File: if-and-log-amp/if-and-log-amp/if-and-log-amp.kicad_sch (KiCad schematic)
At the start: 84 parts, among them J301 Coax, J302 SMA Panel Mount, J303 SMA Panel Mount, J304 SMA Panel Mount, J305 Conn_01x03, J306 Conn_01x02, J307 Conn_Coaxial, Q301 2N3904, T301 FT37-43 8:2 t, U301 AD603AQ, U302 L78L05_TO92, U303 LM317L_TO92, U304 ${SIM.PARAMS}, U305 CA3140

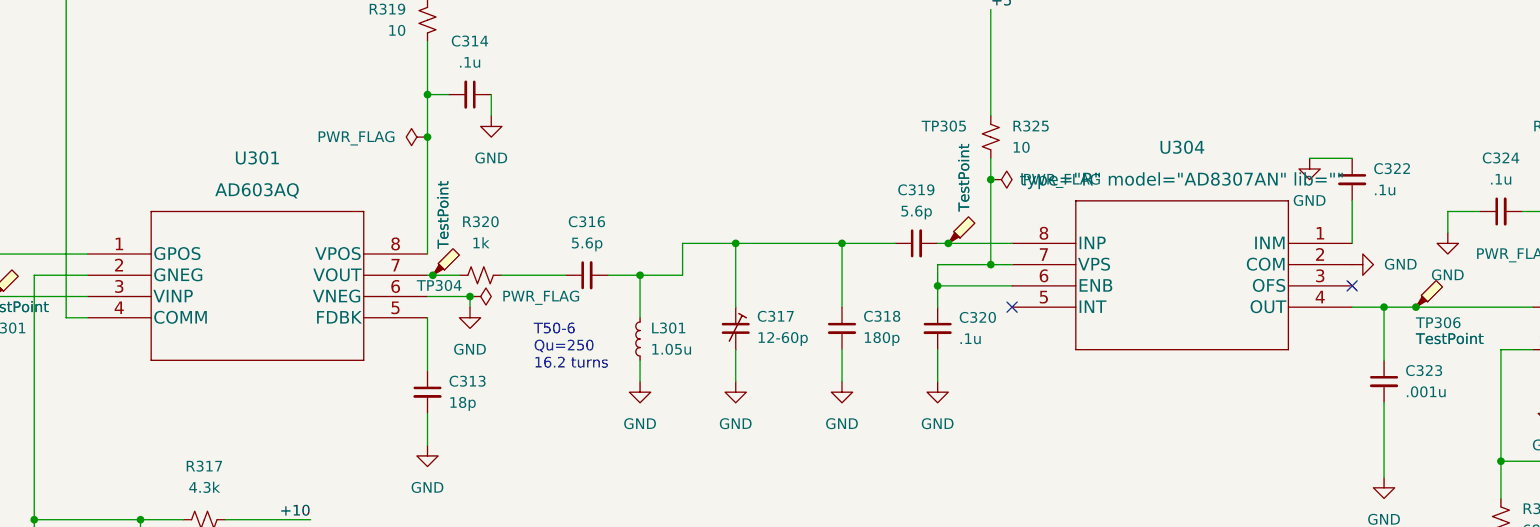
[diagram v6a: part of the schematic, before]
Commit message: Update to timebase and 2lo gerbers
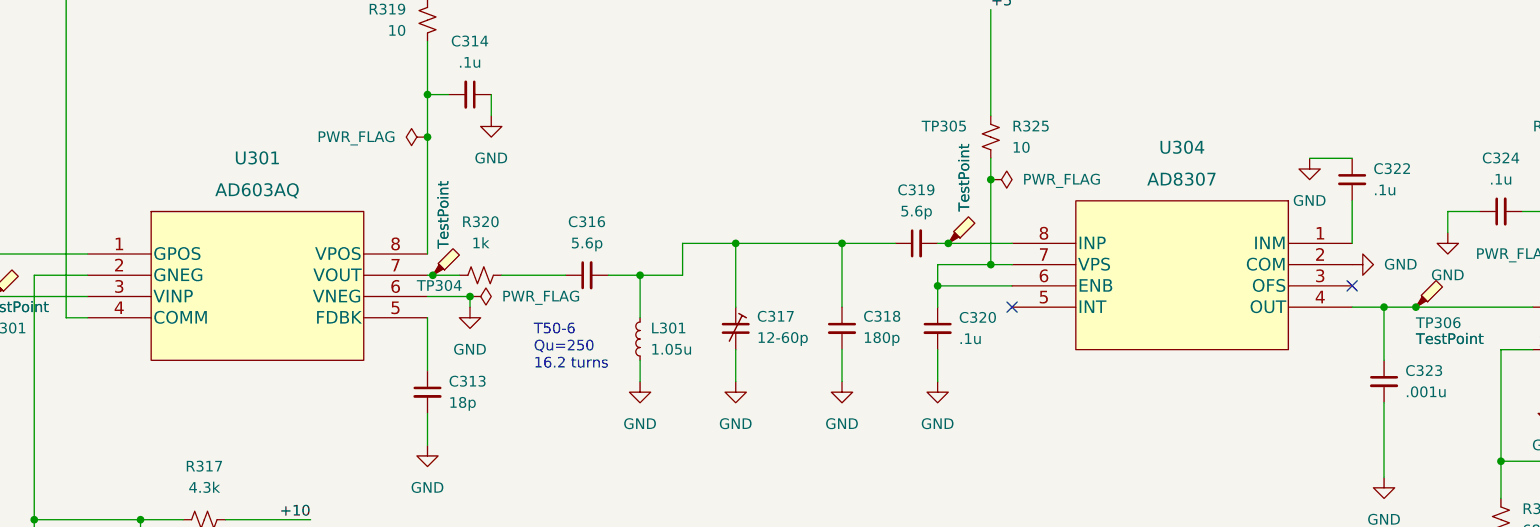
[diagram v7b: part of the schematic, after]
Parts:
- U301: footprint if-log-amp:AD603AQ -> Q_8_ADI; symbol AD603AQ:AD603AQ -> spectrum analyzer:AD603AQ
- U304: value ${SIM.PARAMS} -> AD8307; footprint if-log-amp:AD8307AN -> N_8_ADI; symbol AD8307AN:AD8307AN -> spectrum analyzer:AD8307AN
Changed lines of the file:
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@@
     )
   )
-  (symbol (lib_id "AD8307AN:AD8307AN") (at 252.73 62.23 0) (mirror y) (unit 1)
+  (symbol (lib_id "spectrum analyzer:AD8307AN") (at 252.73 62.23 0) (mirror y) (unit 1)
     (in_bom yes) (on_board yes) (dnp no) (fields_autoplaced)
     (property "Reference" "U304" (at 232.41 50.8 0)
       (effects (font (size 1.524 1.524)))
     )
-    (property "Value" "${SIM.PARAMS}" (at 232.41 54.61 0)
+    (property "Value" "AD8307" (at 232.41 54.61 0)
       (effects (font (size 1.524 1.524)))
     )
-    (property "Footprint" "if-log-amp:AD8307AN" (at 232.41 56.134 0)
+    (property "Footprint" "N_8_ADI" (at 232.41 56.134 0)
       (effects (font (size 1.524 1.524)) hide)
     )
@@
       (effects (font (size 1.524 1.524)) hide)
     )
-    (property "Sim.Enable" "0" (at 252.73 62.23 0)
-      (effects (font (size 1.27 1.27)) hide)
-    )
-    (property "Sim.Device" "SPICE" (at 252.73 62.23 0)
-      (effects (font (size 1.27 1.27)) hide)
-    )
-    (property "Sim.Params" "type=\"R\" model=\"AD8307AN\" lib=\"\"" (at 0 0 0)
+    (property "Sim.Device" "SUBCKT" (at 252.73 62.23 0)
+      (effects (font (size 1.27 1.27)) hide)
+    )
+    (property "Sim.Pins" "1=8 2=1 3=5 4=3 5=4 6=6 7=7" (at 0 0 0)
       (effects (font (size 0 0)) hide)
     )
-    (property "Sim.Pins" "1=1 2=2 3=3 4=4 5=5 6=6 7=7 8=8" (at 0 0 0)
-      (effects (font (size 0 0)) hide)
+    (property "Sim.Name" "AD8310_MODEL" (at 252.73 62.23 0)
+      (effects (font (size 1.27 1.27)) hide)
+    )
+    (property "Sim.Library" "if-log-amp-spice\\ad8310_SUBCKT.cir" (at 252.73 62.23 0)
+      (effects (font (size 1.27 1.27)) hide)
     )
     (pin "1")
@@
     )
   )
-  (symbol (lib_id "AD603AQ:AD603AQ") (at 101.6 63.5 0) (unit 1)
+  (symbol (lib_id "spectrum analyzer:AD603AQ") (at 101.6 63.5 0) (unit 1)
     (in_bom yes) (on_board yes) (dnp no) (fields_autoplaced)
     (property "Reference" "U301" (at 121.92 52.07 0)
@@
       (effects (font (size 1.524 1.524)))
     )
-    (property "Footprint" "if-log-amp:AD603AQ" (at 121.92 57.404 0)
+    (property "Footprint" "Q_8_ADI" (at 121.92 57.404 0)
       (effects (font (size 1.524 1.524)) hide)
     )
